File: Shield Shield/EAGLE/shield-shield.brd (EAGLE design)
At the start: 93.7 x 53.3 mm, 20 parts, among them IC1 MC33269D-5.0, J1 POWER_JACKSLT, U1 TXB0108PWR, U2 TXB0108PWR

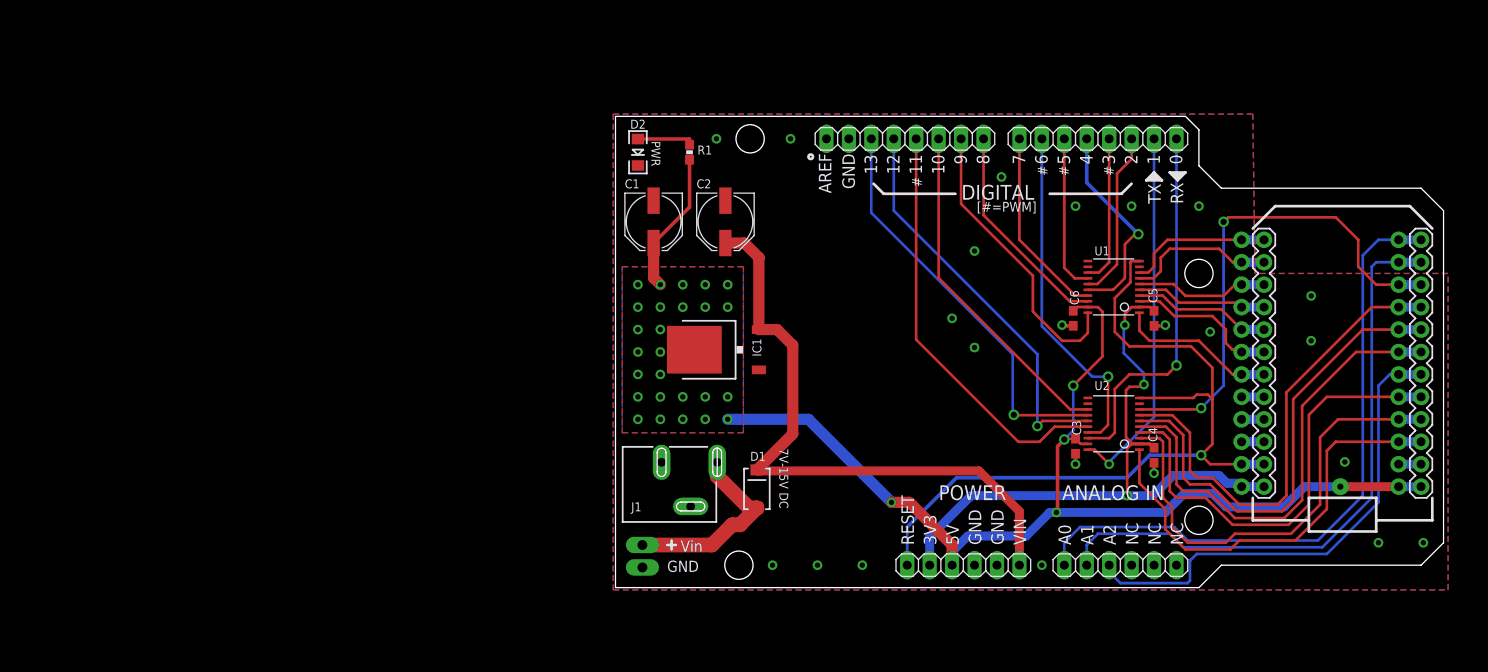
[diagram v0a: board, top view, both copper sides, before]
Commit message: updated shield BOMs and boards
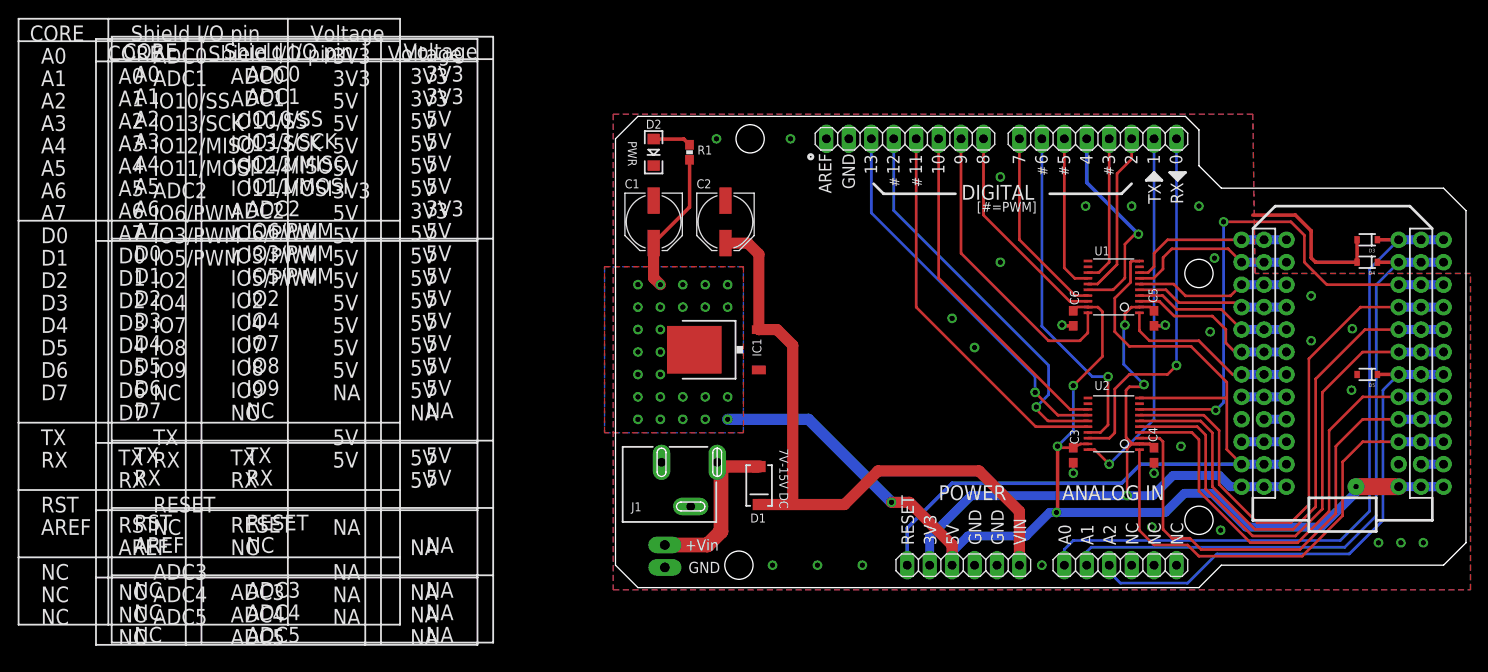
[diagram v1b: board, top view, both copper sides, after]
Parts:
- added D3, D4, D5: DIODE-ZENER-BZT52, SparkFun-DiscreteSemi:SOD-323
- added LOGO1: OSHW-LOGOM, Spark:OSHW-LOGO-M
- moved U$2 48.5 mm to (-5.16, 49.4), flipped to the bottom
- moved JP1 2.54 mm to (5.59, 4.83)
- moved D2 1.78 mm to (4.32, 49.3)
- moved C3 1.05 mm to (51.8, 15.0)
- moved D1 0.46 mm to (16.3, 11.6), turned to 270 degrees
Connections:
- net +3V3: now also U$1.#24
- net +5V: now also U$1.#1
- net A2: now also U$1.#10
- net A3: now also U$1.#9
- net A4: now also U$1.#8
- net A5: now also U$1.#7
- net A7: now also U$1.#5
- net AD0: now also D3.1, U$1.#12
- net AD1: now also D4.1, U$1.#11
- net AD2: now also D5.1, U$1.#6
- net D7: now also U$1.#20
- net GND: now also D3.2, D4.2, D5.2, U$1.#2, U$1.#21
- net N$1: now also U$1.#19
- net N$2: now also U$1.#18
- net N$3: now also U$1.#17
- net N$4: now also U$1.#16
- net N$5: now also U$1.#15
- net N$6: now also U$1.#14
- net N$7: now also U$1.#13
- net RESET: now also U$1.#23
- net RX: now also U$1.#4
- net TX: now also U$1.#3
- net VDDA: now also U$1.#22
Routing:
- net GND: track 10.2 -> 28.5 mm, vias 23 -> 29
- net A3: track 54.7 -> 62.8 mm
- net +5V: track 140.2 -> 148.2 mm
- net A4: track 54.2 -> 60.9 mm
- net A5: track 53.3 -> 59.5 mm
- net AD1: track 70.0 -> 75.8 mm
- net TX: track 49.0 -> 53.7 mm
- net RESET: track 90.2 -> 94.8 mm, vias 1 -> 0
- net AD2: track 55.5 -> 60.0 mm
- net RX: track 52.1 -> 56.0 mm
- net VIN: track 70.8 -> 74.5 mm
- net MOSI: track 47.7 -> 44.1 mm
- net AD0: track 74.3 -> 77.7 mm
- net A2: track 56.7 -> 60.0 mm
- net A7: track 52.1 -> 55.2 mm
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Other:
- board size 93.7 x 53.3 mm -> 96.3 x 53.3 mm
- board text added: "+Vin"
- board text added: "0 1 2 3 4 5 6 7 8 9 10 11 12 13 A0 A1 A2 AREF RESET VIN 5V 3V3 NC"
- board text added: "5V 5V 5V 5V 5V 5V 5V 5V 5V 5V 5V 5V 5V 5V 3V3 3V3 3V3 NA 3V3 15V 5V 3V3 NA"
- board text added: "A3"
- board text added: "A4"
- board text added: "A5"
- board text added: "A6"
- board text added: "A7"
- board text added: "ADC0"
- board text added: "ADC1"
- board text added: "ADC2"
- board text added: "ADC3"
- board text added: "ADC4"
- board text added: "ADC5"
- board text added: "CORE"
- board text added: "D0"
- board text added: "D1"
- board text added: "D2"
- board text added: "D3"
- board text added: "D4"
- board text added: "D5"
- board text added: "D6"
- board text added: "D7"
- board text added: "FUNCTION"
- board text added: "IO/RX IO/TX IO IO/PWM IO IO/PWM IO/PWM IO IO IO IO/SS IO/PWM/MOSI IO/PWM/MISO IO/SCK IO/ANALOG IO/ANALOG IO/ANALOG NC CORE RESET INPUT VOLTAGE 5V OUT 3V3 OUT NOT CONNECTED"
- board text added: "IO10/SS"
- board text added: "IO11/MOSI"
- board text added: "IO12/MISO"
- board text added: "IO13/SCK"
- board text added: "IO2"
- board text added: "IO3/PWM"
- board text added: "IO4"
- board text added: "IO5/PWM"
- board text added: "IO6/PWM"
- board text added: "IO7"
- board text added: "IO8"
- board text added: "IO9"
- board text added: "MAX VOL"
- board text added: "NA"
- board text added: "RST"
- board text added: "SHIELD PINS"
- board text added: "Shield I/O pin"
- board text added: "Shield Shield V2.0"
- board text added: "Voltage"
- board text removed: "Spark Shield Shield"
- board text removed: "Vin"

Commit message: added resistors to the sshield and some minor edits
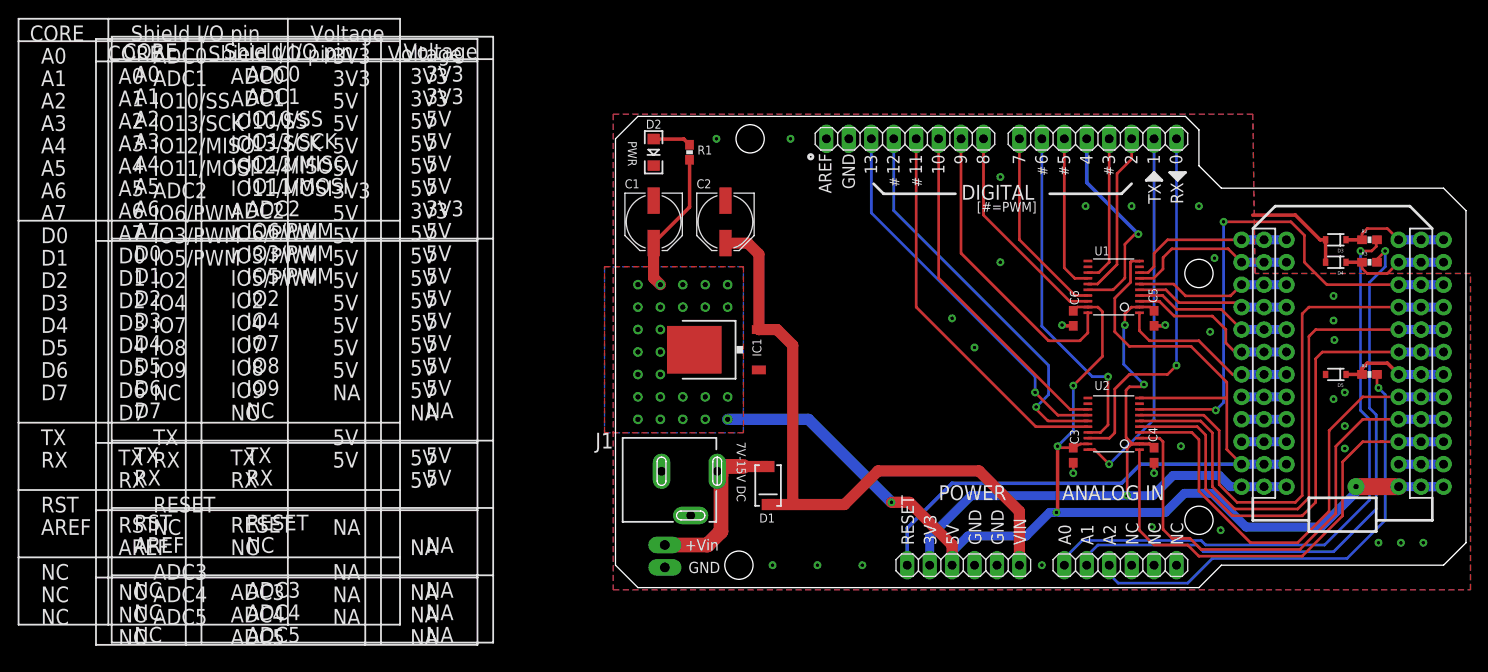
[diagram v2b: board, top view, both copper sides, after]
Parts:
- removed U$2: (no value), Spark:SPARK_LOGO
- added R2, R3, R4: 150, SparkFun-Passives:0603-RES
- added U$3: SPARK_LOGO, Spark:SPARK_LOGO_TSTOP
- J1: device SparkFun-Connectors:POWER_JACK_SLOT -> Spark:POWER_JACK_SLOT
- moved D3 3.56 mm to (81.5, 39.4)
- moved D4 3.56 mm to (81.5, 36.8)
- moved D5 3.56 mm to (81.5, 24.1)
- moved J1 1.02 mm to (-2.29, 15.7)
- moved D1 1.02 mm to (17.3, 11.6)
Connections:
- new net N$10: AD.1, R2.2
- new net N$11: AD.2, R3.2
- new net N$12: AD.3, R4.2
- net AD0: now also R2.1; no longer AD.1
- net AD1: now also R3.1; no longer AD.2
- net AD2: now also R4.1; no longer AD.3
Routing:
- net N$10: track 0.00 -> 69.9 mm, vias 0 -> 1
- net N$11: track 0.00 -> 68.5 mm, vias 0 -> 1
- net AD0: track 77.7 -> 12.5 mm
- net AD1: track 75.8 -> 15.0 mm
- net N$12: track 0.00 -> 52.5 mm, vias 0 -> 1
- net AD2: track 60.0 -> 12.5 mm
- net GND: track 28.5 -> 27.2 mm, vias 29 -> 32
- net VIN: track 74.5 -> 73.5 mm
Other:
- board text added: "Shield Shield v2.0 sparkdevices.com"
- board text removed: "Shield Shield V2.0"

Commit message: added license info to all design files
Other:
- board text added: "Reference Designs ARE PROVIDED "AS IS" AND "WITH ALL FAULTS. SPARK LABS, INC ("SPARK") DISCLAIMS ALL OTHER WARRANTIES, EXPRESS OR IMPLIED, REGARDING PRODUCTS OR THE REFERENCE DESIGNS, INCLUDING BUT NOT LIMITED TO, ANY IMPLIED WARRANTIES OF MERCHANTABILITY, FITNESS FOR A PARTICULAR PURPOSE, OR NON-INFRINGEMENT. Spark may make changes to specifications and product descriptions at any time, without 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"
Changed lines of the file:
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@@
 <setting verticaltext="up"/>
 </settings>
-<grid distance="0.05" unitdist="inch" unit="inch" style="lines" multiple="1" display="yes" altdistance="0.05" altunitdist="inch" altunit="inch"/>
+<grid distance="0.1" unitdist="inch" unit="inch" style="lines" multiple="1" display="yes" altdistance="0.05" altunitdist="inch" altunit="inch"/>
 <layers>
 <layer number="1" name="Top" color="4" fill="1" visible="yes" active="yes"/>
@@
 NOT CONNECTED
 </text>
+<text x="121.92" y="5.08" size="1.778" layer="51">Reference Designs ARE PROVIDED "AS IS" AND "WITH ALL FAULTS. SPARK LABS, INC
+("SPARK") DISCLAIMS ALL OTHER WARRANTIES, EXPRESS OR IMPLIED, REGARDING
+PRODUCTS OR THE REFERENCE DESIGNS, INCLUDING BUT NOT LIMITED TO, ANY
+IMPLIED WARRANTIES OF MERCHANTABILITY, FITNESS FOR A PARTICULAR PURPOSE,
+ OR NON-INFRINGEMENT.
+Spark may make changes to specifications and product descriptions at any
+time, without notice. The Customer must not rely on the absence or
+characteristics of any features or instructions marked "reserved" or
+"undefined." Spark reserves these for future definition and shall have
+no responsibility whatsoever for conflicts or incompatibilities arising
+from future changes to them. The product information on the Web Site or
+Materials is subject to change without notice. Do not finalize a design
+with this information.
+Spark is a registered trademark.</text>
+<wire x1="119.38" y1="0" x2="119.38" y2="53.34" width="0.4064" layer="51"/>
+<wire x1="119.38" y1="53.34" x2="243.84" y2="53.34" width="0.4064" layer="51"/>
+<wire x1="243.84" y1="53.34" x2="243.84" y2="0" width="0.4064" layer="51"/>
+<wire x1="243.84" y1="0" x2="119.38" y2="0" width="0.4064" layer="51"/>
 </plain>
 <attributes>
@@
 </signal>
 </signals>
-<errors>
-</errors>
 </board>
 </drawing>

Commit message: updated sshield and pshield gerbers
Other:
- board text added: "Shield Shield v2.0.1 spark.io"
- board text removed: "Shield Shield v2.0 sparkdevices.com"
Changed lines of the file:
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@@
 <?xml version="1.0" encoding="utf-8"?>
 <!DOCTYPE eagle SYSTEM "eagle.dtd">
-<eagle version="6.3">
+<eagle version="6.5.0">
 <drawing>
 <settings>
@@
 <layer number="27" name="tValues" color="7" fill="1" visible="no" active="yes"/>
 <layer number="28" name="bValues" color="7" fill="1" visible="no" active="yes"/>
-<layer number="29" name="tStop" color="2" fill="3" visible="yes" active="yes"/>
+<layer number="29" name="tStop" color="2" fill="3" visible="no" active="yes"/>
 <layer number="30" name="bStop" color="5" fill="6" visible="no" active="yes"/>
 <layer number="31" name="tCream" color="7" fill="4" visible="no" active="yes"/>
@@
 <layer number="50" name="ReferenceLS" color="12" fill="1" visible="no" active="yes"/>
 <layer number="51" name="tDocu" color="6" fill="1" visible="yes" active="yes"/>
-<layer number="52" name="bDocu" color="7" fill="1" visible="yes" active="yes"/>
+<layer number="52" name="bDocu" color="7" fill="1" visible="no" active="yes"/>
 <layer number="57" name="tCAD" color="7" fill="1" visible="no" active="no"/>
 <layer number="91" name="Nets" color="2" fill="1" visible="no" active="no"/>
@@
 <hole x="15.24" y="50.8" drill="3.2"/>
 <hole x="13.97" y="2.54" drill="3.2"/>
-<text x="77.216" y="12.446" size="1.778" layer="22" font="vector" ratio="15" rot="MR90">Shield Shield v2.0
-sparkdevices.com
+<text x="77.216" y="12.446" size="1.778" layer="22" font="vector" ratio="15" rot="MR90">Shield Shield v2.0.1
+spark.io
 </text>
 <wire x1="68.58" y1="2.54" x2="93.726" y2="2.54" width="0" layer="20"/>
@@
 <wire x1="26.67" y1="7.62" x2="26.67" y2="34.29" width="0.2032" layer="22"/>
 <wire x1="20.32" y1="7.62" x2="20.32" y2="34.29" width="0.2032" layer="22"/>
-<dimension x1="96.266" y1="42.672" x2="0" y2="46.482" x3="48.133" y3="56.642" layer="51" dtype="horizontal"/>
-<dimension x1="2.54" y1="0" x2="2.54" y2="53.34" x3="-5.588" y3="26.67" layer="51" dtype="vertical"/>
+<dimension x1="96.266" y1="42.672" x2="0" y2="46.482" x3="48.133" y3="56.642" textsize="3.5" layer="51" dtype="horizontal"/>
+<dimension x1="2.54" y1="0" x2="2.54" y2="53.34" x3="-5.588" y3="26.67" textsize="3.5" layer="51" dtype="vertical"/>
 <text x="16.51" y="8.89" size="1.016" layer="22" ratio="15" rot="MR90">0
 1
